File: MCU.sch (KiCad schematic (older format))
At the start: 14 parts, among them J6 Conn_01x02, J7 AVR-ISP-6, Q3 MMBT3904, SW2 SW_SPDT, U4 ATtiny13-20SSU

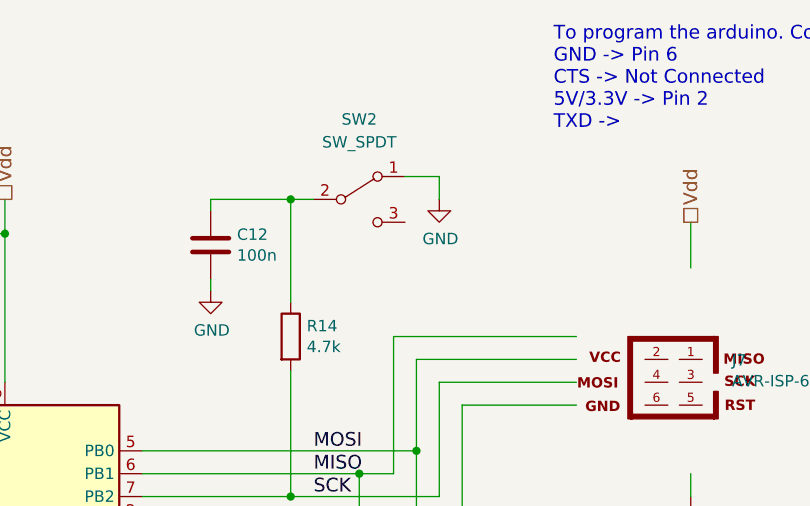
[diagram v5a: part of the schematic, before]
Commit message: Added power on state LED Updated to KiCAD 5.0
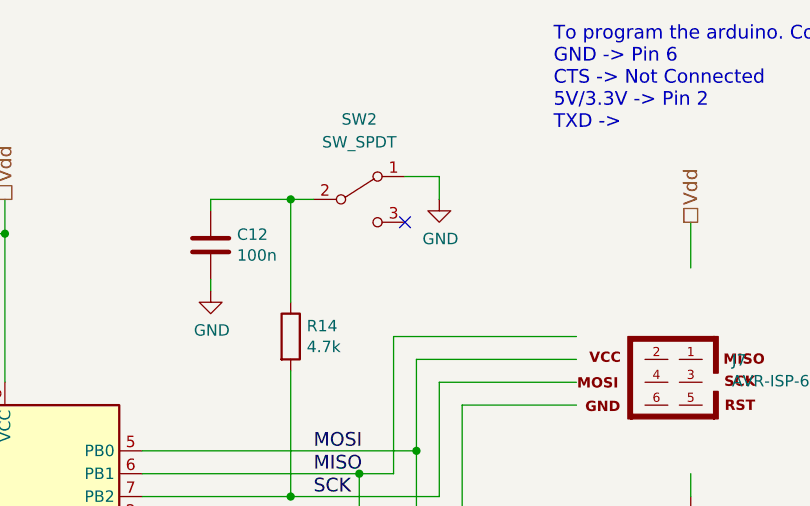
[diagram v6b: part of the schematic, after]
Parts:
- C10, C11, C12: footprint Capacitors_SMD:C_0603 -> Capacitor_SMD:C_0603_1608Metric
- Q3: footprint TO_SOT_Packages_SMD:SOT-23 -> Package_TO_SOT_SMD:SOT-23
- R13, R14, R15, R16, R17, R18: footprint Resistors_SMD:R_0603 -> Resistor_SMD:R_0603_1608Metric
- SW2: footprint Buttons_Switches_THT:SW_CuK_OS102011MA1QN1_SPDT_Angled -> Button_Switch_THT:SW_CuK_OS102011MA1QN1_SPDT_Angled
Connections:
- no-connect marks 0 -> 1
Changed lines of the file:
@@
 F 0 "R13" V 5343 4550 50  0000 C CNN
 F 1 "1k" V 5434 4550 50  0000 C CNN
-F 2 "Resistors_SMD:R_0603" V 5480 4550 50  0001 C CNN
+F 2 "Resistor_SMD:R_0603_1608Metric" V 5480 4550 50  0001 C CNN
 F 3 "" H 5550 4550 50  0001 C CNN
 F 4 "Yageo" H 5550 4550 60  0001 C CNN "MFN"
@@
 F 0 "C11" H 5965 4846 50  0000 L CNN
 F 1 "100n" H 5965 4755 50  0000 L CNN
-F 2 "Capacitors_SMD:C_0603" H 5888 4650 50  0001 C CNN
+F 2 "Capacitor_SMD:C_0603_1608Metric" H 5888 4650 50  0001 C CNN
 F 3 "" H 5850 4800 50  0001 C CNN
 F 4 "Murata" H 5850 4800 60  0001 C CNN "MFN"
@@
 F 0 "R16" H 9070 2946 50  0000 L CNN
 F 1 "10k" H 9070 2855 50  0000 L CNN
-F 2 "Resistors_SMD:R_0603" V 8930 2900 50  0001 C CNN
+F 2 "Resistor_SMD:R_0603_1608Metric" V 8930 2900 50  0001 C CNN
 F 3 "" H 9000 2900 50  0001 C CNN
 F 4 "Yageo" H 9000 2900 60  0001 C CNN "MFN"
@@
 F 0 "C10" H 4815 2296 50  0000 L CNN
 F 1 "100n" H 4815 2205 50  0000 L CNN
-F 2 "Capacitors_SMD:C_0603" H 4738 2100 50  0001 C CNN
+F 2 "Capacitor_SMD:C_0603_1608Metric" H 4738 2100 50  0001 C CNN
 F 3 "" H 4700 2250 50  0001 C CNN
 F 4 "Murata" H 4700 2250 60  0001 C CNN "MFN"
@@
 F 0 "R15" H 8720 4896 50  0000 L CNN
 F 1 "470" H 8720 4805 50  0000 L CNN
-F 2 "Resistors_SMD:R_0603" V 8580 4850 50  0001 C CNN
+F 2 "Resistor_SMD:R_0603_1608Metric" V 8580 4850 50  0001 C CNN
 F 3 "" H 8650 4850 50  0001 C CNN
 F 4 "Yageo" H 8650 4850 60  0001 C CNN "MFN"
@@
 F 0 "SW2" H 6700 2250 50  0000 C CNN
 F 1 "SW_SPDT" H 6700 2150 50  0000 C CNN
-F 2 "Buttons_Switches_THT:SW_CuK_OS102011MA1QN1_SPDT_Angled" H 6700 1900 50  0001 C CNN
+F 2 "Button_Switch_THT:SW_CuK_OS102011MA1QN1_SPDT_Angled" H 6700 1900 50  0001 C CNN
 F 3 "" H 6700 1900 50  0001 C CNN
 F 4 "C&K Components" H 6700 1900 60  0001 C CNN "MFN"
@@
 F 0 "C12" H 6165 2146 50  0000 L CNN
 F 1 "100n" H 6165 2055 50  0000 L CNN
-F 2 "Capacitors_SMD:C_0603" H 6088 1950 50  0001 C CNN
+F 2 "Capacitor_SMD:C_0603_1608Metric" H 6088 1950 50  0001 C CNN
 F 3 "" H 6050 2100 50  0001 C CNN
 F 4 "Murata" H 6050 2100 60  0001 C CNN "MFN"
@@
 F 0 "R14" H 6470 2546 50  0000 L CNN
 F 1 "4.7k" H 6470 2455 50  0000 L CNN
-F 2 "Resistors_SMD:R_0603" V 6330 2500 50  0001 C CNN
+F 2 "Resistor_SMD:R_0603_1608Metric" V 6330 2500 50  0001 C CNN
 F 3 "" H 6400 2500 50  0001 C CNN
 F 4 "Yageo" H 6400 2500 60  0001 C CNN "MFN"
@@
 F 0 "R17" V 7593 4050 50  0000 C CNN
 F 1 "4.7k" V 7684 4050 50  0000 C CNN
-F 2 "Resistors_SMD:R_0603" V 7730 4050 50  0001 C CNN
+F 2 "Resistor_SMD:R_0603_1608Metric" V 7730 4050 50  0001 C CNN
 F 3 "" H 7800 4050 50  0001 C CNN
 F 4 "Yageo" H 7800 4050 50  0001 C CNN "MFN"
@@
 F 0 "Q3" H 8741 5596 50  0000 L CNN
 F 1 "MMBT3904" H 8741 5505 50  0000 L CNN
-F 2 "TO_SOT_Packages_SMD:SOT-23" H 8750 5475 50  0001 L CIN
+F 2 "Package_TO_SOT_SMD:SOT-23" H 8750 5475 50  0001 L CIN
 F 3 "" H 8550 5550 50  0001 L CNN
 F 4 "Nexperia" H 8550 5550 50  0001 C CNN "MFN"
@@
 F 0 "R18" V 7843 5550 50  0000 C CNN
 F 1 "4.7k" V 7934 5550 50  0000 C CNN
-F 2 "Resistors_SMD:R_0603" V 7980 5550 50  0001 C CNN
+F 2 "Resistor_SMD:R_0603_1608Metric" V 7980 5550 50  0001 C CNN
 F 3 "" H 8050 5550 50  0001 C CNN
 F 4 "Yageo" H 8050 5550 50  0001 C CNN "MFN"
@@
 Text HLabel 9000 2500 1    60   UnSpc ~ 0
 Vdd
+NoConn ~ 6900 2000
 $EndSCHEMATC

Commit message: Added part numbers Updated BOM
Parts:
- U4: MFN (none) -> Atmel; MFP (none) -> ATtiny13-20SSU
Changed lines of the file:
@@
 F 2 "Package_SO:SOIC-8_3.9x4.9mm_P1.27mm" H 5150 3300 50  0001 C CIN
 F 3 "http://ww1.microchip.com/downloads/en/DeviceDoc/doc2535.pdf" H 5150 3300 50  0001 C CNN
+F 4 "Atmel" H 5150 3300 50  0001 C CNN "MFN"
+F 5 "ATtiny13-20SSU" H 5150 3300 50  0001 C CNN "MFP"
 	1    5150 3300
 	1    0    0    -1
